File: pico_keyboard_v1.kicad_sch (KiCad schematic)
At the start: 9 parts, among them J1 Conn_01x04_12864, J2 Conn_01x03_Female, SW1 RotaryEncoder_Switch, U1 COM-09032, U2 Pico

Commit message: More changes
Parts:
- added C1, C2: 0.01 μF, Capacitor_SMD:C_1206_3216Metric_Pad1.33x1.80mm_HandSolder, symbol Device:C
- added R3, R4: 10k, Resistor_THT:R_Axial_DIN0207_L6.3mm_D2.5mm_P10.16mm_Horizontal, symbol Device:R
- U2: footprint RPi_Pico:RPi_Pico_SMD_TH -> MCU_RaspberryPi_and_Boards:RPi_Pico_SMD_TH
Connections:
- net +3V3: no longer R1.2, R2.2
- net +5V: now also R1.2, R2.2
- net GND: now also C1.2, C2.1
- net GPIO19: now also C1.1, R3.2; no longer SW1.A
- net GPIO22: now also C2.2, R4.2; no longer SW1.B
- new net: R4.1, SW1.B
- new net: R3.1, SW1.A
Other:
- moved on the sheet: R1, R2

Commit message: Draft
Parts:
- J1: footprint Connector_PinHeader_2.00mm:PinHeader_1x04_P2.00mm_Vertical -> Connector_PinHeader_2.54mm:PinHeader_1x04_P2.54mm_Vertical
- J2: footprint Connector_PinHeader_2.00mm:PinHeader_1x03_P2.00mm_Vertical -> Connector_PinHeader_2.54mm:PinHeader_1x03_P2.54mm_Vertical
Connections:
- net NC: no longer names the net of U1.S1 (SHIELD), U1.S2 (SHIELD), U1.S3 (SHIELD), U1.S4 (SHIELD)
- net NC: no longer U2.30 (RUN), U2.33 (AGND), U2.35 (ADC_VREF), U2.37 (3V3_EN)
- no-connect marks 0 -> 5
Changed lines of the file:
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@@
   (junction (at 179.578 69.342) (diameter 0) (color 0 0 0 0)
   )
+  (no_connect (at 229.108 59.182))
+  (no_connect (at 229.108 64.262))
+  (no_connect (at 229.108 76.962))
+  (no_connect (at 229.108 69.342))
+  (no_connect (at 67.818 136.652))
   (wire (pts (xy 146.558 59.182) (xy 152.908 59.182))
     (stroke (width 0) (type default) (color 0 0 0 0))
@@
     )
   )
-  (global_label "NC" (shape input) (at 229.108 76.962 0) (fields_autoplaced)
-    (effects (font (size 1.27 1.27)) (justify left))
-    (property "Intersheet References" "${INTERSHEET_REFS}" (id 0) (at 234.1216 76.8826 0)
-      (effects (font (size 1.27 1.27)) (justify left) hide)
-    )
-  )
   (global_label "C9" (shape input) (at 146.558 64.262 180) (fields_autoplaced)
     (effects (font (size 1.27 1.27)) (justify right))
@@
     )
   )
-  (global_label "NC" (shape input) (at 67.818 136.652 180) (fields_autoplaced)
-    (effects (font (size 1.27 1.27)) (justify right))
-    (property "Intersheet References" "${INTERSHEET_REFS}" (id 0) (at 62.8044 136.7314 0)
-      (effects (font (size 1.27 1.27)) (justify right) hide)
-    )
-  )
   (global_label "C3" (shape input) (at 146.558 49.022 180) (fields_autoplaced)
     (effects (font (size 1.27 1.27)) (justify right))
@@
     )
   )
-  (global_label "NC" (shape input) (at 229.108 69.342 0) (fields_autoplaced)
-    (effects (font (size 1.27 1.27)) (justify left))
-    (property "Intersheet References" "${INTERSHEET_REFS}" (id 0) (at 234.1216 69.2626 0)
-      (effects (font (size 1.27 1.27)) (justify left) hide)
-    )
-  )
   (global_label "GPIO0" (shape input) (at 152.908 41.402 0) (fields_autoplaced)
     (effects (font (size 1.27 1.27)) (justify left))
@@
     )
   )
-  (global_label "NC" (shape input) (at 229.108 64.262 0) (fields_autoplaced)
-    (effects (font (size 1.27 1.27)) (justify left))
-    (property "Intersheet References" "${INTERSHEET_REFS}" (id 0) (at 234.1216 64.1826 0)
-      (effects (font (size 1.27 1.27)) (justify left) hide)
-    )
-  )
   (global_label "GPIO19" (shape input) (at 133.096 108.712 0) (fields_autoplaced)
     (effects (font (size 1.27 1.27)) (justify left))
@@
     (effects (font (size 1.27 1.27)) (justify left))
     (property "Intersheet References" "${INTERSHEET_REFS}" (id 0) (at 161.0059 76.8826 0)
-      (effects (font (size 1.27 1.27)) (justify left) hide)
-    )
-  )
-  (global_label "NC" (shape input) (at 229.108 59.182 0) (fields_autoplaced)
-    (effects (font (size 1.27 1.27)) (justify left))
-    (property "Intersheet References" "${INTERSHEET_REFS}" (id 0) (at 234.1216 59.1026 0)
       (effects (font (size 1.27 1.27)) (justify left) hide)
     )
@@
   (symbol (lib_id "Connector:Conn_01x04_Female") (at 98.298 65.532 0) (unit 1)
     (in_bom yes) (on_board yes) (fields_autoplaced)
-    (property "Reference" "J1" (id 0) (at 99.568 65.5319 0)
+    (property "Reference" "J1" (id 0) (at 99.06 65.5319 0)
       (effects (font (size 1.27 1.27)) (justify left))
     )
-    (property "Value" "Conn_01x04_12864" (id 1) (at 99.568 68.0719 0)
+    (property "Value" "Conn_01x04_12864" (id 1) (at 99.06 68.0719 0)
       (effects (font (size 1.27 1.27)) (justify left))
     )
-    (property "Footprint" "Connector_PinHeader_2.00mm:PinHeader_1x04_P2.00mm_Vertical" (id 2) (at 98.298 65.532 0)
+    (property "Footprint" "Connector_PinHeader_2.54mm:PinHeader_1x04_P2.54mm_Vertical" (id 2) (at 98.298 65.532 0)
       (effects (font (size 1.27 1.27)) hide)
     )
@@
   (symbol (lib_id "Connector:Conn_01x03_Female") (at 211.328 116.967 270) (unit 1)
     (in_bom yes) (on_board yes) (fields_autoplaced)
-    (property "Reference" "J2" (id 0) (at 211.328 120.142 90))
-    (property "Value" "Conn_01x03_Female" (id 1) (at 211.328 122.682 90))
-    (property "Footprint" "Connector_PinHeader_2.00mm:PinHeader_1x03_P2.00mm_Vertical" (id 2) (at 211.328 116.967 0)
+    (property "Reference" "J2" (id 0) (at 211.328 119.38 90))
+    (property "Value" "Conn_01x03_Female" (id 1) (at 211.328 121.92 90))
+    (property "Footprint" "Connector_PinHeader_2.54mm:PinHeader_1x03_P2.54mm_Vertical" (id 2) (at 211.328 116.967 0)
       (effects (font (size 1.27 1.27)) hide)
     )
@@
       (reference "D55") (unit 1) (value "D") (footprint "Diode_THT:D_DO-35_SOD27_P7.62mm_Horizontal")
     )
-    (path "/93eb0ca5-32f0-4914-ab02-ab34a84786ac/87cbff27-b1e6-4738-b02d-19f9d0413c6b"
-      (reference "D56") (unit 1) (value "D") (footprint "Diode_THT:D_DO-35_SOD27_P7.62mm_Horizontal")
-    )
     (path "/93eb0ca5-32f0-4914-ab02-ab34a84786ac/c6443d90-7cb2-47bd-865f-13cdaa7bc2c9"
       (reference "D57") (unit 1) (value "D") (footprint "Diode_THT:D_DO-35_SOD27_P7.62mm_Horizontal")
@@
     )
     (path "/b89f738e-8c3e-40c9-b2a7-408e8e95e3d1"
-      (reference "J1") (unit 1) (value "Conn_01x04_12864") (footprint "Connector_PinHeader_2.00mm:PinHeader_1x04_P2.00mm_Vertical")
+      (reference "J1") (unit 1) (value "Conn_01x04_12864") (footprint "Connector_PinHeader_2.54mm:PinHeader_1x04_P2.54mm_Vertical")
     )
     (path "/d3f790aa-d4b9-4890-be7f-b9e9dd8e4a6f"
-      (reference "J2") (unit 1) (value "Conn_01x03_Female") (footprint "Connector_PinHeader_2.00mm:PinHeader_1x03_P2.00mm_Vertical")
+      (reference "J2") (unit 1) (value "Conn_01x03_Female") (footprint "Connector_PinHeader_2.54mm:PinHeader_1x03_P2.54mm_Vertical")
     )
     (path "/3bea3cce-39c1-447f-b376-6f5a68806cd5"
@@
       (reference "SW54") (unit 1) (value "SW_/") (footprint "Switch_Keyboard_Hotswap_Kailh:SW_Hotswap_Kailh_MX_1.00u")
     )
-    (path "/93eb0ca5-32f0-4914-ab02-ab34a84786ac/b8a5ccb7-3fcb-4d54-8af6-ff2a503e0eba"
-      (reference "SW55") (unit 1) (value "SW_fn2") (footprint "Switch_Keyboard_Hotswap_Kailh:SW_Hotswap_Kailh_MX_1.00u")
-    )
     (path "/93eb0ca5-32f0-4914-ab02-ab34a84786ac/e2fbfb68-2502-4201-8729-9318b4333f5b"
       (reference "SW56") (unit 1) (value "SW_-") (footprint "Switch_Keyboard_Hotswap_Kailh:SW_Hotswap_Kailh_MX_1.00u")
@@
     )
     (path "/93eb0ca5-32f0-4914-ab02-ab34a84786ac/d41c3382-c4cf-4e32-a54b-d56382f31061"
-      (reference "SW67") (unit 1) (value "SW_\\") (footprint "Switch_Keyboard_Hotswap_Kailh:SW_Hotswap_Kailh_MX_1.00u")
+      (reference "SW67") (unit 1) (value "SW_\\") (footprint "Switch_Keyboard_Hotswap_Kailh:SW_Hotswap_Kailh_MX_1.50u")
     )
     (path "/93eb0ca5-32f0-4914-ab02-ab34a84786ac/8bce7f83-aa81-431e-adf7-862cdb185361"

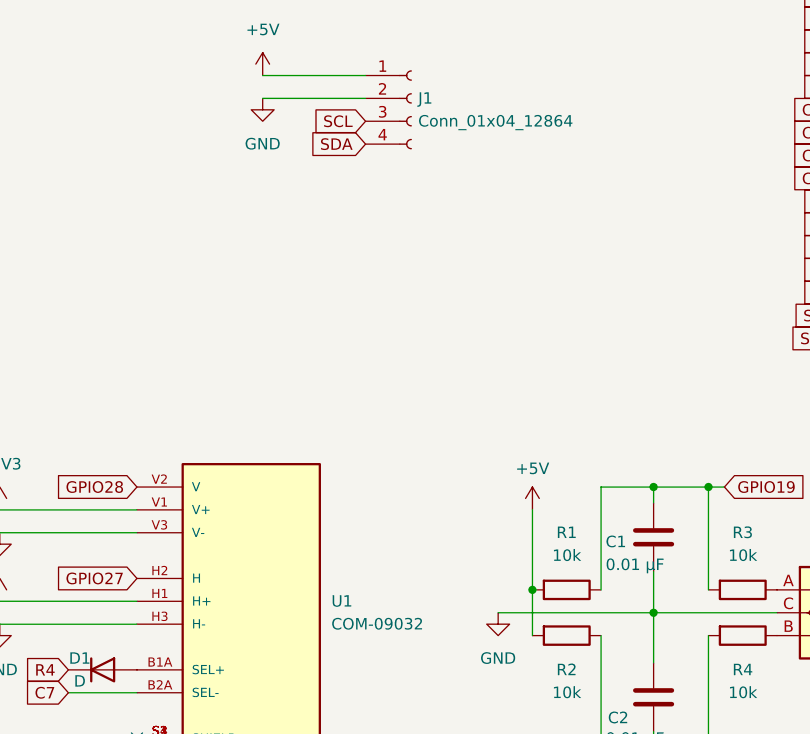
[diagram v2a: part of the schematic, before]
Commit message: More polished. Added mounting hole and led
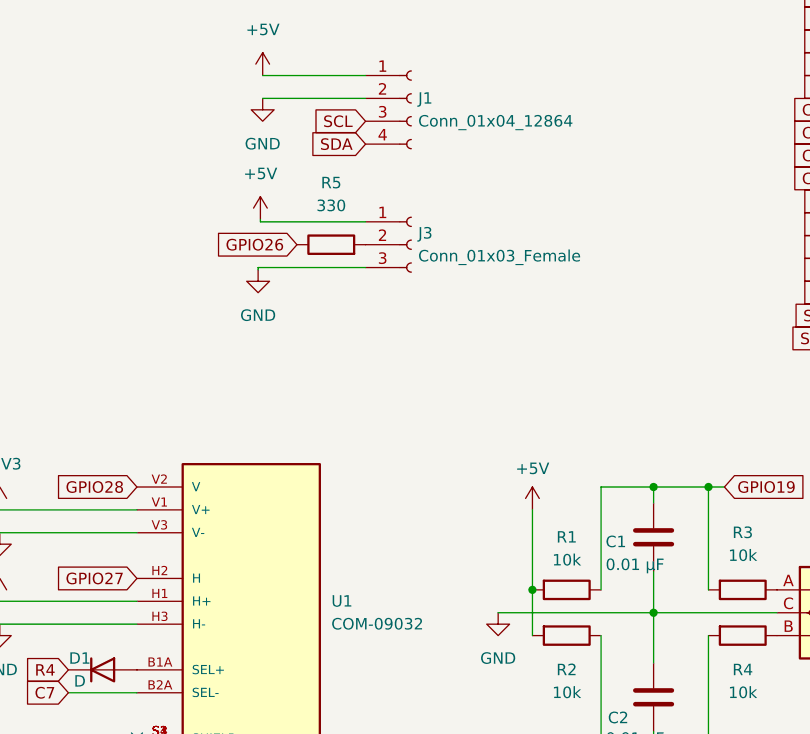
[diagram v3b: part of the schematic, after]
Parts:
- added J3: Conn_01x03_Female, Connector_PinHeader_2.54mm:PinHeader_1x03_P2.54mm_Vertical, symbol Connector:Conn_01x03_Female
- added R5: 330, Resistor_THT:R_Axial_DIN0207_L6.3mm_D2.5mm_P10.16mm_Horizontal, symbol Device:R
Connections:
- net +5V: now also J3.1 (Pin_1)
- net GND: now also J3.3 (Pin_3)
- net GPIO26: now also R5.1
- new net: J3.2 (Pin_2), R5.2
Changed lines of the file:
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@@
+    (stroke (width 0) (type default) (color 0 0 0 0))
+  )
+  (wire (pts (xy 93.218 84.328) (xy 81.28 84.328))
+    (stroke (width 0) (type default) (color 0 0 0 0))
+  )
+  (wire (pts (xy 93.218 79.248) (xy 81.534 79.248))
     (stroke (width 0) (type default) (color 0 0 0 0))
   )
@@
     (stroke (width 0) (type default) (color 0 0 0 0))
   )
+  (wire (pts (xy 81.534 79.248) (xy 81.534 78.994))
+    (stroke (width 0) (type default) (color 0 0 0 0))
+  )
   (wire (pts (xy 146.558 82.042) (xy 152.908 82.042))
     (stroke (width 0) (type default) (color 0 0 0 0))
@@
     (stroke (width 0) (type default) (color 0 0 0 0))
   )
+  (wire (pts (xy 81.28 84.328) (xy 81.28 84.582))
+    (stroke (width 0) (type default) (color 0 0 0 0))
+  )
   (wire (pts (xy 146.558 56.642) (xy 152.908 56.642))
     (stroke (width 0) (type default) (color 0 0 0 0))
@@
     (property "Intersheet References" "${INTERSHEET_REFS}" (id 0) (at 238.4154 87.0426 0)
       (effects (font (size 1.27 1.27)) (justify left) hide)
+    )
+  )
+  (global_label "GPIO26" (shape input) (at 85.598 81.788 180) (fields_autoplaced)
+    (effects (font (size 1.27 1.27)) (justify right))
+    (property "Intersheet References" "${INTERSHEET_REFS}" (id 0) (at 76.2906 81.8674 0)
+      (effects (font (size 1.27 1.27)) (justify right) hide)
     )
   )
@@
     (pin "1")
   )
+  (symbol (lib_id "power:GND") (at 81.28 84.582 0) (unit 1)
+    (in_bom yes) (on_board yes) (fields_autoplaced)
+    (property "Reference" "#PWR016" (id 0) (at 81.28 90.932 0)
+      (effects (font (size 1.27 1.27)) hide)
+    )
+    (property "Value" "GND" (id 1) (at 81.28 89.662 0))
+    (property "Footprint" "" (id 2) (at 81.28 84.582 0)
+      (effects (font (size 1.27 1.27)) hide)
+    )
+    (property "Datasheet" "" (id 3) (at 81.28 84.582 0)
+      (effects (font (size 1.27 1.27)) hide)
+    )
+    (pin "1")
+  )
+  (symbol (lib_id "Connector:Conn_01x03_Female") (at 98.298 81.788 0) (unit 1)
+    (in_bom yes) (on_board yes) (fields_autoplaced)
+    (property "Reference" "J3" (id 0) (at 99.06 80.5179 0)
+      (effects (font (size 1.27 1.27)) (justify left))
+    )
+    (property "Value" "Conn_01x03_Female" (id 1) (at 99.06 83.0579 0)
+      (effects (font (size 1.27 1.27)) (justify left))
+    )
+    (property "Footprint" "Connector_PinHeader_2.54mm:PinHeader_1x03_P2.54mm_Vertical" (id 2) (at 98.298 81.788 0)
+      (effects (font (size 1.27 1.27)) hide)
+    )
+    (property "Datasheet" "~" (id 3) (at 98.298 81.788 0)
+      (effects (font (size 1.27 1.27)) hide)
+    )
+    (pin "1")
+    (pin "2")
+    (pin "3")
+  )
   (symbol (lib_id "Device:D") (at 157.988 125.222 180) (unit 1)
     (in_bom yes) (on_board yes) (fields_autoplaced)
@@
   (symbol (lib_id "Device:R") (at 115.57 120.142 270) (unit 1)
     (in_bom yes) (on_board yes) (fields_autoplaced)
-    (property "Reference" "R1" (id 0) (at 115.57 113.792 90))
-    (property "Value" "10k" (id 1) (at 115.57 116.332 90))
+    (property "Reference" "R1" (id 0) (at 115.57 114.3 90))
+    (property "Value" "10k" (id 1) (at 115.57 116.84 90))
     (property "Footprint" "Resistor_THT:R_Axial_DIN0207_L6.3mm_D2.5mm_P10.16mm_Horizontal" (id 2) (at 115.57 118.364 90)
       (effects (font (size 1.27 1.27)) hide)
@@
     )
     (property "Datasheet" "~" (id 3) (at 125.222 114.3 0)
+      (effects (font (size 1.27 1.27)) hide)
+    )
+    (pin "1")
+    (pin "2")
+  )
+  (symbol (lib_id "Device:R") (at 89.408 81.788 90) (unit 1)
+    (in_bom yes) (on_board yes) (fields_autoplaced)
+    (property "Reference" "R5" (id 0) (at 89.408 74.93 90))
+    (property "Value" "330" (id 1) (at 89.408 77.47 90))
+    (property "Footprint" "Resistor_THT:R_Axial_DIN0207_L6.3mm_D2.5mm_P10.16mm_Horizontal" (id 2) (at 89.408 83.566 90)
+      (effects (font (size 1.27 1.27)) hide)
+    )
+    (property "Datasheet" "~" (id 3) (at 89.408 81.788 0)
       (effects (font (size 1.27 1.27)) hide)
     )
@@
     (pin "9")
   )
+  (symbol (lib_id "power:+5V") (at 81.534 78.994 0) (unit 1)
+    (in_bom yes) (on_board yes) (fields_autoplaced)
+    (property "Reference" "#PWR017" (id 0) (at 81.534 82.804 0)
+      (effects (font (size 1.27 1.27)) hide)
+    )
+    (property "Value" "+5V" (id 1) (at 81.534 73.914 0))
+    (property "Footprint" "" (id 2) (at 81.534 78.994 0)
+      (effects (font (size 1.27 1.27)) hide)
+    )
+    (property "Datasheet" "" (id 3) (at 81.534 78.994 0)
+      (effects (font (size 1.27 1.27)) hide)
+    )
+    (pin "1")
+  )
   (symbol (lib_id "power:GND") (at 245.618 94.742 0) (unit 1)
     (in_bom yes) (on_board yes) (fields_autoplaced)
@@
       (reference "#PWR015") (unit 1) (value "GND") (footprint "")
     )
+    (path "/1cb4f8f9-bdeb-4899-990b-96e347e0353c"
+      (reference "#PWR016") (unit 1) (value "GND") (footprint "")
+    )
+    (path "/ac40eaf1-15fa-474a-a0f7-557ebd34d760"
+      (reference "#PWR017") (unit 1) (value "+5V") (footprint "")
+    )
     (path "/6543cff2-97b1-415a-aaf5-93a0dc83f814"
       (reference "C1") (unit 1) (value "0.01 μF") (footprint "Capacitor_SMD:C_1206_3216Metric_Pad1.33x1.80mm_HandSolder")
@@
       (reference "J2") (unit 1) (value "Conn_01x03_Female") (footprint "Connector_PinHeader_2.54mm:PinHeader_1x03_P2.54mm_Vertical")
     )
+    (path "/29f8f16e-f080-4d77-9976-065de9c61964"
+      (reference "J3") (unit 1) (value "Conn_01x03_Female") (footprint "Connector_PinHeader_2.54mm:PinHeader_1x03_P2.54mm_Vertical")
+    )
     (path "/3bea3cce-39c1-447f-b376-6f5a68806cd5"
       (reference "R1") (unit 1) (value "10k") (footprint "Resistor_THT:R_Axial_DIN0207_L6.3mm_D2.5mm_P10.16mm_Horizontal")
@@
       (reference "R4") (unit 1) (value "10k") (footprint "Resistor_THT:R_Axial_DIN0207_L6.3mm_D2.5mm_P10.16mm_Horizontal")
     )
+    (path "/656f3247-8fb9-4d4b-9016-264f42a3b801"
+      (reference "R5") (unit 1) (value "330") (footprint "Resistor_THT:R_Axial_DIN0207_L6.3mm_D2.5mm_P10.16mm_Horizontal")
+    )
     (path "/ee94c2d8-91ca-4111-a04a-bdf7da8ba7c3"

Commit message: V1, before a major change
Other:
- title: (none) -> Pico Prototype Keyboard 65%
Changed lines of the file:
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@@
 (kicad_sch (version 20211123) (generator eeschema)
   (paper "A4")
+  (title_block
+    (title "Pico Prototype Keyboard 65%")
+    (comment 1 "Ver 0.1")
+    (comment 2 "CC BY-SA 2.0")
+  )
   (junction (at 233.172 51.562) (diameter 0) (color 0 0 0 0)
   )
@@
     )
     (path "/93eb0ca5-32f0-4914-ab02-ab34a84786ac/a32f2533-40ef-41b2-84eb-34fda6dad253"
-      (reference "SW45") (unit 1) (value "SW_r_ctrl") (footprint "Switch_Keyboard_Hotswap_Kailh:SW_Hotswap_Kailh_MX_1.00u")
+      (reference "SW45") (unit 1) (value "SW_fn1") (footprint "Switch_Keyboard_Hotswap_Kailh:SW_Hotswap_Kailh_MX_1.00u")
     )
     (path "/93eb0ca5-32f0-4914-ab02-ab34a84786ac/08072c06-3ca4-4152-917a-c4b4aad9a172"
@@
     )
     (path "/93eb0ca5-32f0-4914-ab02-ab34a84786ac/76372b8e-8496-4c93-868a-5cd38f8ac61d"
-      (reference "SW50") (unit 1) (value "SW_fn1") (footprint "Switch_Keyboard_Hotswap_Kailh:SW_Hotswap_Kailh_MX_1.00u")
+      (reference "SW50") (unit 1) (value "SW_fn2") (footprint "Switch_Keyboard_Hotswap_Kailh:SW_Hotswap_Kailh_MX_1.00u")
     )
     (path "/93eb0ca5-32f0-4914-ab02-ab34a84786ac/bee60033-38f1-4cde-8722-374ed59cb68a"

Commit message: New version
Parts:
- J1: footprint Connector_PinHeader_2.54mm:PinHeader_1x04_P2.54mm_Vertical -> JMD0.96C:JMD0.96C
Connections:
- net C4: now also U1.B2A (SEL-)
- net C7: no longer U1.B2A (SEL-)
- net GPIO16: now also D2.1 (K)
- net GPIO17: no longer D2.1 (K)
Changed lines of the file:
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@@
     )
   )
-  (global_label "C7" (shape input) (at 60.198 131.572 180) (fields_autoplaced)
-    (effects (font (size 1.27 1.27)) (justify right))
-    (property "Intersheet References" "${INTERSHEET_REFS}" (id 0) (at 55.3054 131.6514 0)
+  (global_label "C4" (shape input) (at 60.198 131.572 180) (fields_autoplaced)
+    (effects (font (size 1.27 1.27)) (justify right))
+    (property "Intersheet References" "${INTERSHEET_REFS}" (id 0) (at 55.3054 131.4926 0)
       (effects (font (size 1.27 1.27)) (justify right) hide)
     )
@@
     )
   )
-  (global_label "R3" (shape input) (at 161.798 125.222 0) (fields_autoplaced)
+  (global_label "R2" (shape input) (at 161.798 125.222 0) (fields_autoplaced)
     (effects (font (size 1.27 1.27)) (justify left))
     (property "Intersheet References" "${INTERSHEET_REFS}" (id 0) (at 166.6906 125.1426 0)
@@
       (effects (font (size 1.27 1.27)) (justify left))
     )
-    (property "Footprint" "Connector_PinHeader_2.54mm:PinHeader_1x04_P2.54mm_Vertical" (id 2) (at 98.298 65.532 0)
+    (property "Footprint" "JMD0.96C:JMD0.96C" (id 2) (at 98.298 65.532 0)
       (effects (font (size 1.27 1.27)) hide)
     )
@@
       (reference "D26") (unit 1) (value "D") (footprint "Diode_THT:D_DO-35_SOD27_P7.62mm_Horizontal")
     )
-    (path "/93eb0ca5-32f0-4914-ab02-ab34a84786ac/4d34bcb6-b3ef-4da4-b4bc-aef80fde0b36"
+    (path "/93eb0ca5-32f0-4914-ab02-ab34a84786ac/8cfd8198-2da1-49b2-988a-fc47b5f825b6"
       (reference "D27") (unit 1) (value "D") (footprint "Diode_THT:D_DO-35_SOD27_P7.62mm_Horizontal")
     )
@@
       (reference "D55") (unit 1) (value "D") (footprint "Diode_THT:D_DO-35_SOD27_P7.62mm_Horizontal")
     )
+    (path "/93eb0ca5-32f0-4914-ab02-ab34a84786ac/1da39a32-ecec-495c-8a0e-34e03c6c6dd0"
+      (reference "D56") (unit 1) (value "D") (footprint "Diode_THT:D_DO-35_SOD27_P7.62mm_Horizontal")
+    )
     (path "/93eb0ca5-32f0-4914-ab02-ab34a84786ac/c6443d90-7cb2-47bd-865f-13cdaa7bc2c9"
       (reference "D57") (unit 1) (value "D") (footprint "Diode_THT:D_DO-35_SOD27_P7.62mm_Horizontal")
@@
     )
     (path "/b89f738e-8c3e-40c9-b2a7-408e8e95e3d1"
-      (reference "J1") (unit 1) (value "Conn_01x04_12864") (footprint "Connector_PinHeader_2.54mm:PinHeader_1x04_P2.54mm_Vertical")
+      (reference "J1") (unit 1) (value "Conn_01x04_12864") (footprint "JMD0.96C:JMD0.96C")
     )
     (path "/d3f790aa-d4b9-4890-be7f-b9e9dd8e4a6f"
@@
       (reference "SW25") (unit 1) (value "SW_v") (footprint "Switch_Keyboard_Hotswap_Kailh:SW_Hotswap_Kailh_MX_1.00u")
     )
-    (path "/93eb0ca5-32f0-4914-ab02-ab34a84786ac/7cbf64ab-c826-4e5f-89d7-11e568e4acba"
-      (reference "SW26") (unit 1) (value "SW_m_middle") (footprint "Switch_Keyboard_Hotswap_Kailh:SW_Hotswap_Kailh_MX_1.00u")
+    (path "/93eb0ca5-32f0-4914-ab02-ab34a84786ac/6e8d254a-29e2-433c-a4bb-10fc10c90f8e"
+      (reference "SW26") (unit 1) (value "SW_del") (footprint "Switch_Keyboard_Hotswap_Kailh:SW_Hotswap_Kailh_MX_1.00u")
     )
     (path "/93eb0ca5-32f0-4914-ab02-ab34a84786ac/fd0a5dea-43bd-4651-ba08-f6dc4e249477"
@@
       (reference "SW54") (unit 1) (value "SW_/") (footprint "Switch_Keyboard_Hotswap_Kailh:SW_Hotswap_Kailh_MX_1.00u")
     )
+    (path "/93eb0ca5-32f0-4914-ab02-ab34a84786ac/da0db71c-6006-420e-88af-bf2fc4cfebeb"
+      (reference "SW55") (unit 1) (value "SW_ins") (footprint "Switch_Keyboard_Hotswap_Kailh:SW_Hotswap_Kailh_MX_1.00u")
+    )
     (path "/93eb0ca5-32f0-4914-ab02-ab34a84786ac/e2fbfb68-2502-4201-8729-9318b4333f5b"
       (reference "SW56") (unit 1) (value "SW_-") (footprint "Switch_Keyboard_Hotswap_Kailh:SW_Hotswap_Kailh_MX_1.00u")
@@
     )
     (path "/93eb0ca5-32f0-4914-ab02-ab34a84786ac/3ca8c7fb-316f-4a94-8fcd-84cc752976fa"
-      (reference "SW59") (unit 1) (value "SW_r_shift") (footprint "Switch_Keyboard_Hotswap_Kailh:SW_Hotswap_Kailh_MX_1.75u")
+      (reference "SW59") (unit 1) (value "SW_r_shift") (footprint "Switch_Keyboard_Hotswap_Kailh:SW_Hotswap_Kailh_MX_2.75u")
     )
     (path "/93eb0ca5-32f0-4914-ab02-ab34a84786ac/3e9fcf34-2e40-4689-b87c-54511fefb24c"
@@
     )
     (path "/93eb0ca5-32f0-4914-ab02-ab34a84786ac/95e3c50e-5774-4901-900f-beeed1180985"
-      (reference "SW64") (unit 1) (value "SW_up") (footprint "Switch_Keyboard_Hotswap_Kailh:SW_Hotswap_Kailh_MX_1.00u")
+      (reference "SW64") (unit 1) (value "SW_down") (footprint "Switch_Keyboard_Hotswap_Kailh:SW_Hotswap_Kailh_MX_1.00u")
     )
     (path "/93eb0ca5-32f0-4914-ab02-ab34a84786ac/10889ba4-4543-4360-91d6-dc7d95e4e950"
-      (reference "SW65") (unit 1) (value "SW_down") (footprint "Switch_Keyboard_Hotswap_Kailh:SW_Hotswap_Kailh_MX_1.00u")
+      (reference "SW65") (unit 1) (value "SW_up") (footprint "Switch_Keyboard_Hotswap_Kailh:SW_Hotswap_Kailh_MX_1.00u")
     )
     (path "/93eb0ca5-32f0-4914-ab02-ab34a84786ac/ec14170b-5cf5-4988-b627-513b3c0ee59d"
